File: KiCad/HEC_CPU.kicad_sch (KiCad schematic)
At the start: 10 parts, among them U1 Z80CPU, U11 74LS32, U12 74LS04, U16 74LS32, U20 74LS574, U21 74LS574, U22 74LS02, U6 74LS138, U7 28C256, U8 74LS138

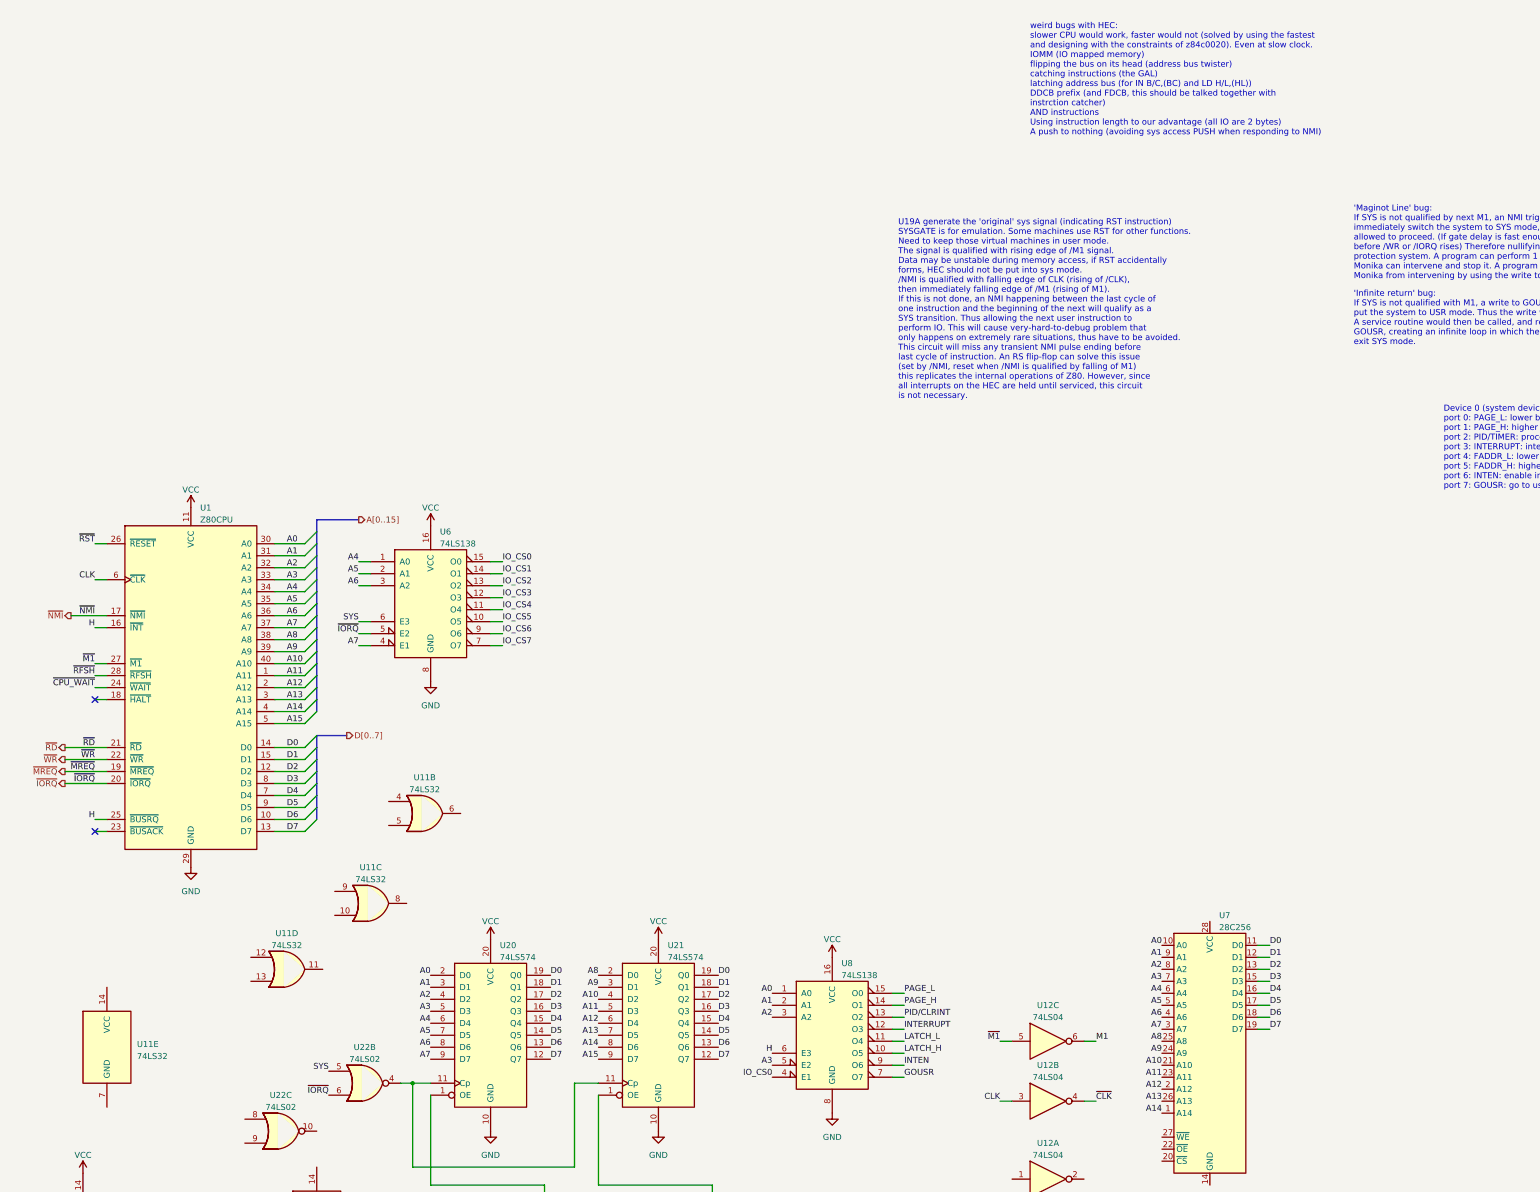
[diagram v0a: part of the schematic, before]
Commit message: Update NMI timing circuit
Updated the NMI generation circuit to prevent a bug occurring when NMI is generated between the rising edge of the last T cycle of an instruction and the falling edge of M1 of the next. Due to delay in M1 signal, the NMI would be qualified one instruction earlier, causing the HEC to enter SYS mode one instruction earlier. If the instruction is an IO instruction by an user program, it can cause a write to any port and potentially destabilize the system.
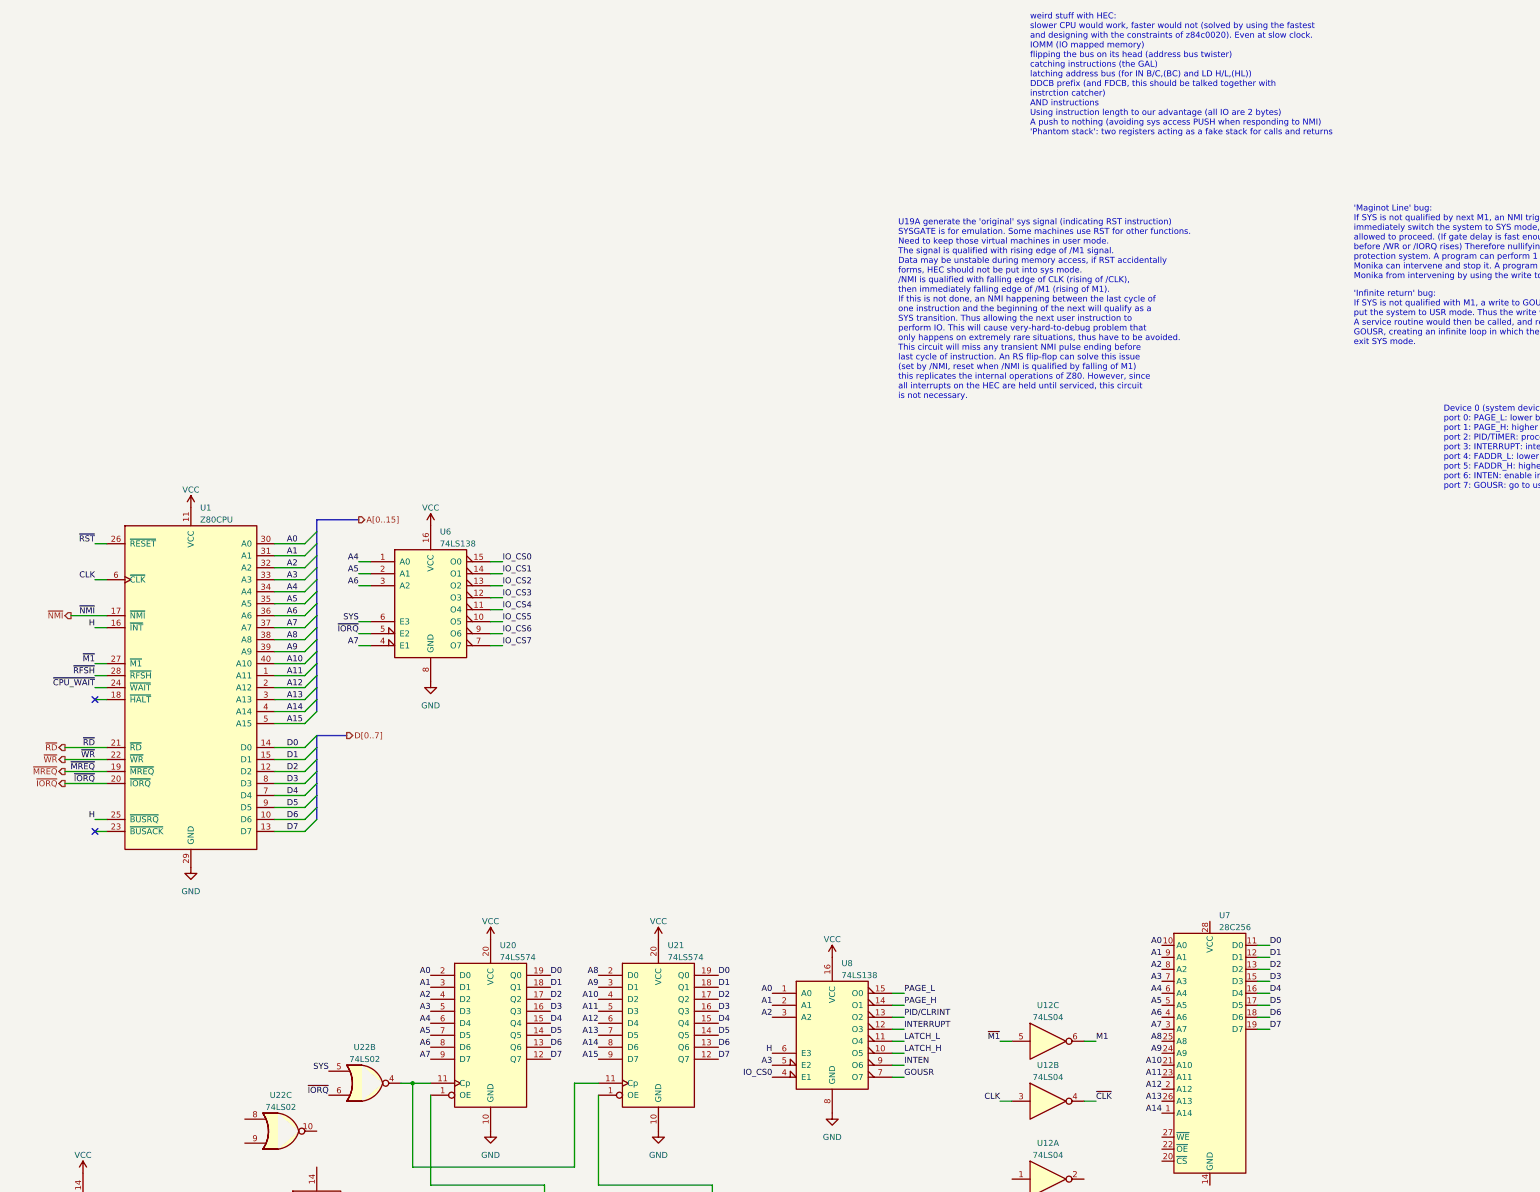
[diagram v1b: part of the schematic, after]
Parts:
- removed U11: 74LS32, Package_DIP:DIP-14_W7.62mm_Socket, symbol 74xx:74LS32
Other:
- note added: "weird stuff with HEC: slower CPU would work, faster would not (solved by using the fastest and designing with the constraints of z84c0020). Even at slow clock. IOMM (IO mapped memory) flipping the bus on its head (address bus twister) catching instructions (the GAL) latching address bus (for IN B/C,(BC) and LD H/L,(HL)) DDCB prefix (and FDCB, this should be talked together with instrction catcher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"
- note removed: "weird bugs with HEC: slower CPU would work, faster would not (solved by using the fastest and designing with the constraints of z84c0020). Even at slow clock. IOMM (IO mapped memory) flipping the bus on its head (address bus twister) catching instructions (the GAL) latching address bus (for IN B/C,(BC) and LD H/L,(HL)) DDCB prefix (and FDCB, this should be talked together with instrction catcher)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"
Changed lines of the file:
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@@
     (effects (font (size 1.27 1.27)) (justify left bottom))
   )
-  (text "weird bugs with HEC:\nslower CPU would work, faster would not (solved by using the fastest\nand designing with the constraints of z84c0020). Even at slow clock.\nIOMM (IO mapped memory)\nflipping the bus on its head (address bus twister)\ncatching instructions (the GAL)\nlatching address bus (for IN B/C,(BC) and LD H/L,(HL))\nDDCB prefix (and FDCB, this should be talked together with \ninstrction catcher)\nAND instructions\nUsing instruction length to our advantage (all IO are 2 bytes)\nA push to nothing (avoiding sys access PUSH when responding to NMI)"
+  (text "weird stuff with HEC:\nslower CPU would work, faster would not (solved by using the fastest\nand designing with the constraints of z84c0020). Even at slow clock.\nIOMM (IO mapped memory)\nflipping the bus on its head (address bus twister)\ncatching instructions (the GAL)\nlatching address bus (for IN B/C,(BC) and LD H/L,(HL))\nDDCB prefix (and FDCB, this should be talked together with \ninstrction catcher)\nAND instructions\nUsing instruction length to our advantage (all IO are 2 bytes)\nA push to nothing (avoiding sys access PUSH when responding to NMI)\n'Phantom stack': two registers acting as a fake stack for calls and returns"
     (at 224.79 -62.23 0)
     (effects (font (size 1.27 1.27)) (justify left bottom))
@@
         (path "/87935374-b60a-4f41-99da-94b76103dd77/73a0c68b-1e42-4c0d-ae31-b1a96d0648bb"
           (reference "U20") (unit 1)
-        )
-      )
-    )
-  )
-  (symbol (lib_id "74xx:74LS32") (at 29.21 130.81 0) (unit 5)
-    (in_bom yes) (on_board yes) (dnp no) (fields_autoplaced)
-    (property "Reference" "U11" (at 35.56 130.175 0)
-      (effects (font (size 1.27 1.27)) (justify left))
-    )
-    (property "Value" "74LS32" (at 35.56 132.715 0)
-      (effects (font (size 1.27 1.27)) (justify left))
-    )
-    (property "Footprint" "Package_DIP:DIP-14_W7.62mm_Socket" (at 29.21 130.81 0)
-      (effects (font (size 1.27 1.27)) hide)
-    )
-    (property "Datasheet" "http://www.ti.com/lit/gpn/sn74LS32" (at 29.21 130.81 0)
-      (effects (font (size 1.27 1.27)) hide)
-    )
-    (pin "1")
-    (pin "2")
-    (pin "3")
-    (pin "4")
-    (pin "5")
-    (pin "6")
-    (pin "10")
-    (pin "8")
-    (pin "9")
-    (pin "11")
-    (pin "12")
-    (pin "13")
-    (pin "14")
-    (pin "7")
-    (instances
-      (project "HEC1"
-        (path "/87935374-b60a-4f41-99da-94b76103dd77/73a0c68b-1e42-4c0d-ae31-b1a96d0648bb"
-          (reference "U11") (unit 5)
         )
       )
@@
         )
       )
-    )
-  )
-  (symbol (lib_id "74xx:74LS32") (at 96.52 81.28 0) (unit 2)
-    (in_bom yes) (on_board yes) (dnp no) (fields_autoplaced)
-    (property "Reference" "U11" (at 96.52 73.66 0)
-      (effects (font (size 1.27 1.27)))
-    )
-    (property "Value" "74LS32" (at 96.52 76.2 0)
-      (effects (font (size 1.27 1.27)))
-    )
-    (property "Footprint" "Package_DIP:DIP-14_W7.62mm_Socket" (at 96.52 81.28 0)
-      (effects (font (size 1.27 1.27)) hide)
-    )
-    (property "Datasheet" "http://www.ti.com/lit/gpn/sn74LS32" (at 96.52 81.28 0)
-      (effects (font (size 1.27 1.27)) hide)
-    )
-    (pin "1")
-    (pin "2")
-    (pin "3")
-    (pin "4")
-    (pin "5")
-    (pin "6")
-    (pin "10")
-    (pin "8")
-    (pin "9")
-    (pin "11")
-    (pin "12")
-    (pin "13")
-    (pin "14")
-    (pin "7")
-    (instances
-      (project "HEC1"
-        (path "/87935374-b60a-4f41-99da-94b76103dd77/73a0c68b-1e42-4c0d-ae31-b1a96d0648bb"
-          (reference "U11") (unit 2)
-        )
-      )
-    )
-  )
-  (symbol (lib_id "74xx:74LS32") (at 85.09 100.33 0) (unit 3)
-    (in_bom yes) (on_board yes) (dnp no) (fields_autoplaced)
-    (property "Reference" "U11" (at 85.09 92.71 0)
-      (effects (font (size 1.27 1.27)))
-    )
-    (property "Value" "74LS32" (at 85.09 95.25 0)
-      (effects (font (size 1.27 1.27)))
-    )
-    (property "Footprint" "Package_DIP:DIP-14_W7.62mm_Socket" (at 85.09 100.33 0)
-      (effects (font (size 1.27 1.27)) hide)
-    )
-    (property "Datasheet" "http://www.ti.com/lit/gpn/sn74LS32" (at 85.09 100.33 0)
-      (effects (font (size 1.27 1.27)) hide)
-    )
-    (pin "1")
-    (pin "2")
-    (pin "3")
-    (pin "4")
-    (pin "5")
-    (pin "6")
-    (pin "10")
-    (pin "8")
-    (pin "9")
-    (pin "11")
-    (pin "12")
-    (pin "13")
-    (pin "14")
-    (pin "7")
-    (instances
-      (project "HEC1"
-        (path "/87935374-b60a-4f41-99da-94b76103dd77/73a0c68b-1e42-4c0d-ae31-b1a96d0648bb"
-          (reference "U11") (unit 3)
-        )
-      )
-    )
-  )
-  (symbol (lib_id "74xx:74LS32") (at 67.31 114.3 0) (unit 4)
-    (in_bom yes) (on_board yes) (dnp no) (fields_autoplaced)
-    (property "Reference" "U11" (at 67.31 106.68 0)
-      (effects (font (size 1.27 1.27)))
-    )
-    (property "Value" "74LS32" (at 67.31 109.22 0)
-      (effects (font (size 1.27 1.27)))
-    )
-    (property "Footprint" "Package_DIP:DIP-14_W7.62mm_Socket" (at 67.31 114.3 0)
-      (effects (font (size 1.27 1.27)) hide)
-    )
-    (property "Datasheet" "http://www.ti.com/lit/gpn/sn74LS32" (at 67.31 114.3 0)
-      (effects (font (size 1.27 1.27)) hide)
-    )
-    (pin "1")
-    (pin "2")
-    (pin "3")
-    (pin "4")
-    (pin "5")
-    (pin "6")
-    (pin "10")
-    (pin "8")
-    (pin "9")
-    (pin "11")
-    (pin "12")
-    (pin "13")
-    (pin "14")
-    (pin "7")
-    (instances
-      (project "HEC1"
-        (path "/87935374-b60a-4f41-99da-94b76103dd77/73a0c68b-1e42-4c0d-ae31-b1a96d0648bb"
-          (reference "U11") (unit 4)
-        )
-      )

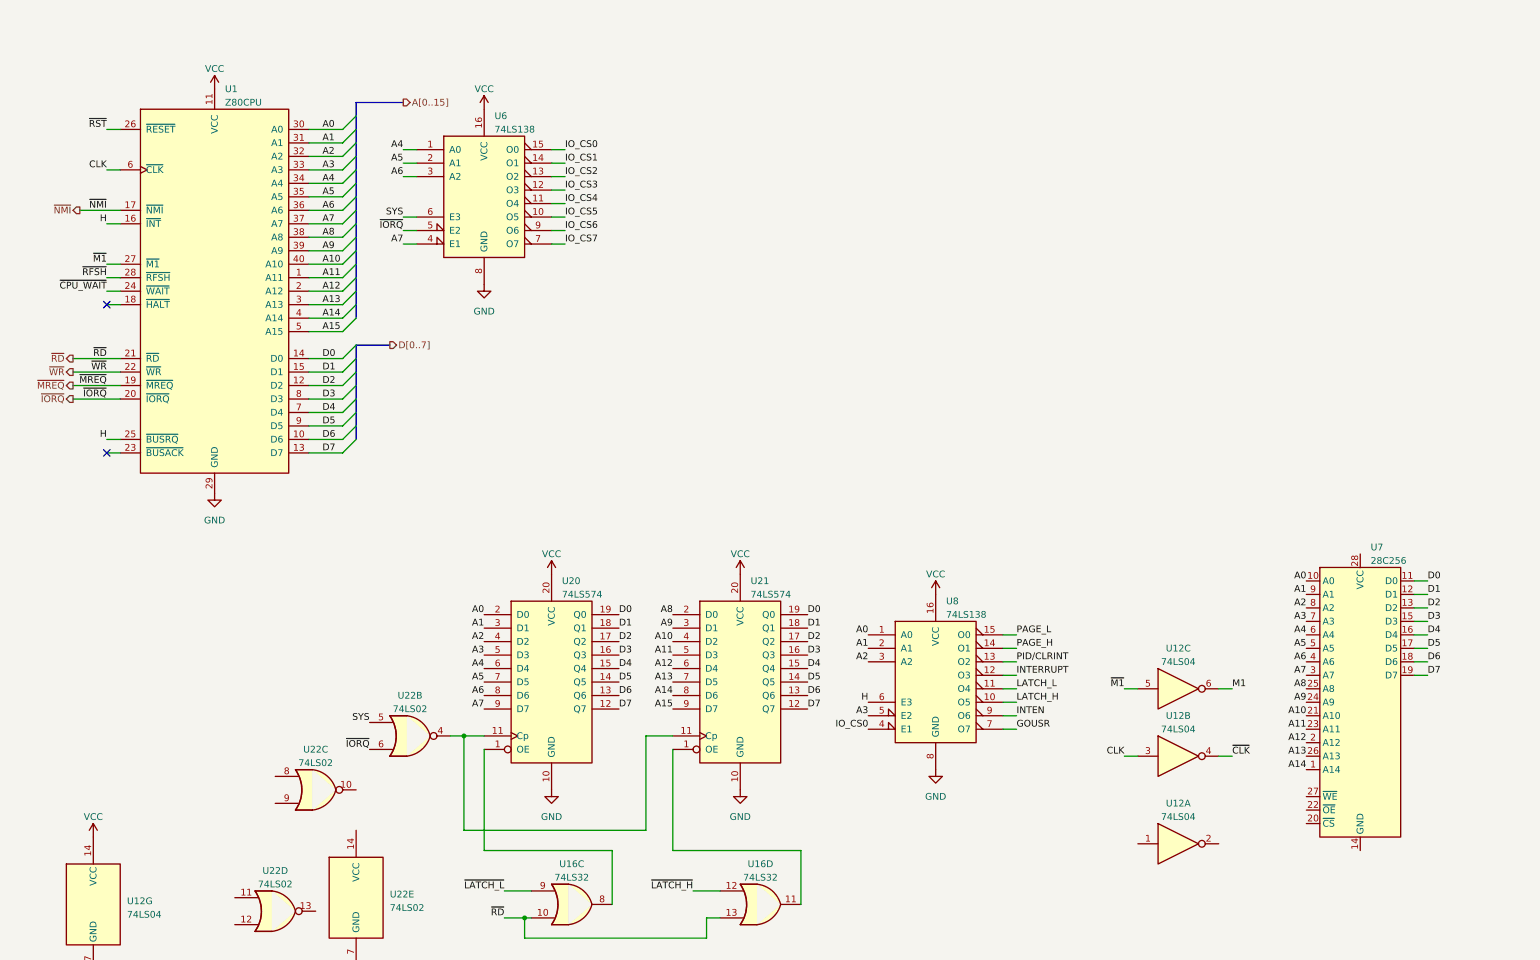
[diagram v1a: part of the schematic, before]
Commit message: Add fault generation circuit
Add circuit to generate fault on illegal read, write and M1 cycle
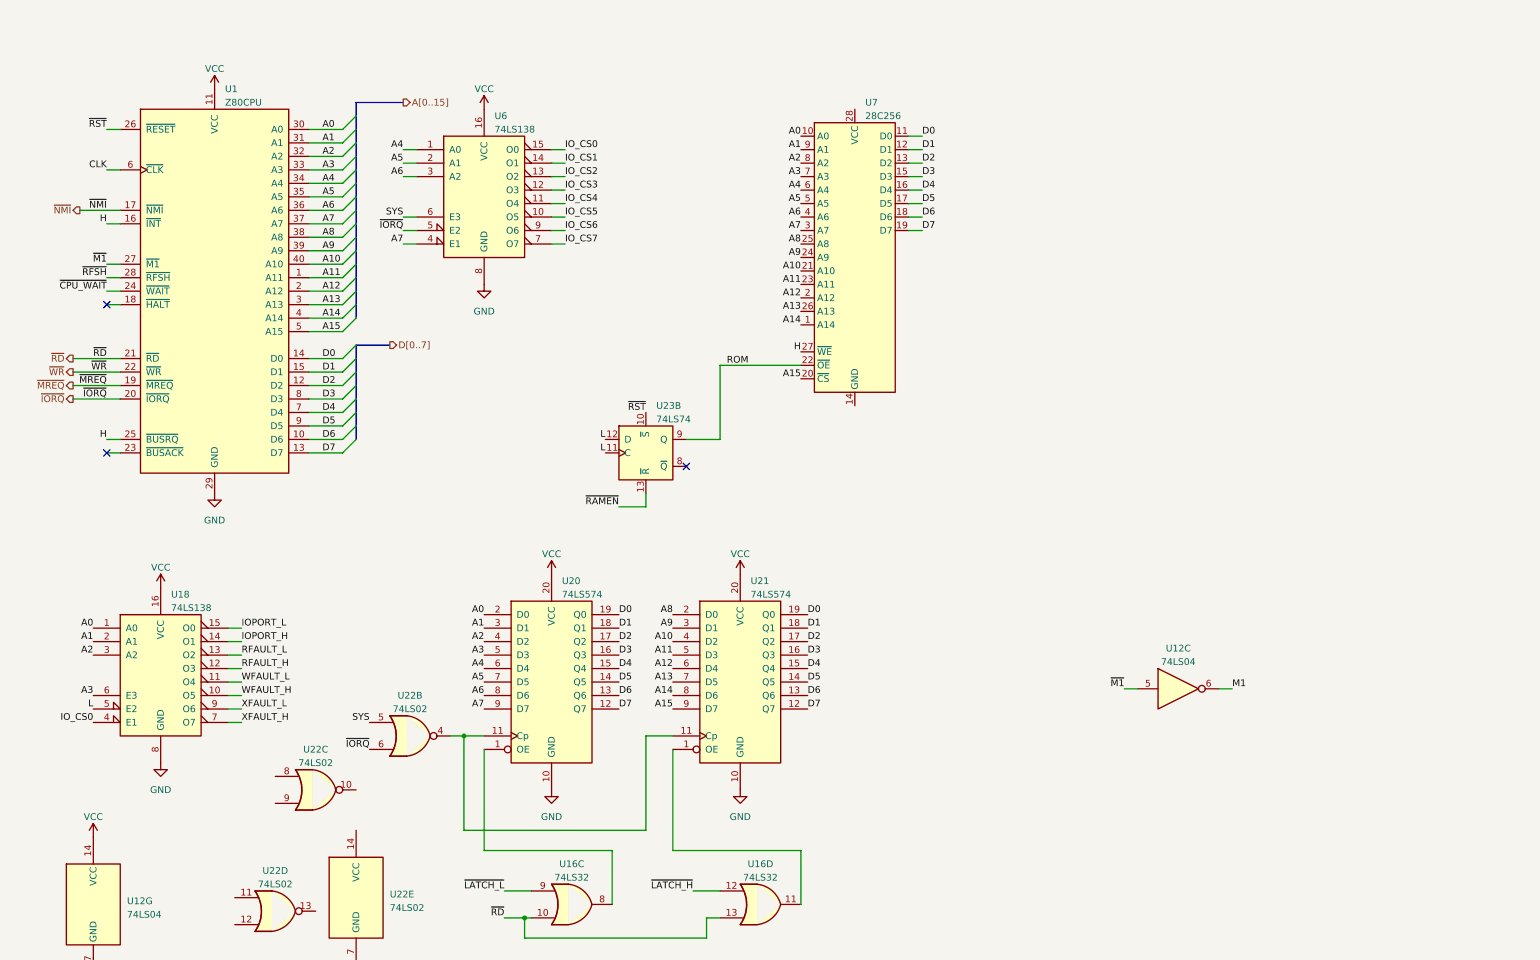
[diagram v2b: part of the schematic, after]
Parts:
- removed unit 1 of U12
- removed unit 2 of U12
- removed U8: 74LS138, Package_DIP:DIP-16_W7.62mm_Socket, symbol 74xx:74LS138
- added U18: 74LS138, symbol 74xx:74LS138
- added U23: 74LS74, Package_DIP:DIP-14_W7.62mm_Socket, symbol 74xx:74LS74
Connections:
- net A0: now also U18.1 (A0)
- net A1: now also U18.2 (A1)
- net A15: now also U7.20 (~{CS})
- net A2: now also U18.3 (A2)
- net A3: now also U18.6 (E3)
- net GND: now also U18.8 (GND)
- net H: now also U7.27 (~{WE})
- net IO_CS0: now also U18.4 (E1)
- net VCC: now also U18.16 (VCC)
- net ~{RST}: now also U23.10 (~{S})
- net ROM: now reaches U7.22 (~{OE})
- net ROM: now also U23.9 (Q)
- new net IOPORT_H: U18.14 (O1)
- new net IOPORT_L: U18.15 (O0)
- new net L: U18.5 (E2), U23.11 (C), U23.12 (D)
- new net RFAULT_H: U18.12 (O3)
- new net RFAULT_L: U18.13 (O2)
- new net WFAULT_H: U18.10 (O5)
- new net WFAULT_L: U18.11 (O4)
- new net XFAULT_H: U18.7 (O7)
- new net XFAULT_L: U18.9 (O6)
- new net ~{RAMEN}: U23.13 (~{R})
- no-connect marks 2 -> 3
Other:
- moved on the sheet: U7
